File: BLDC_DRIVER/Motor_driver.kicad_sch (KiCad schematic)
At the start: 113 parts, among them IC101 DRV8323SRTAR, J104 691311400103, Q101 BSC146N10LS5ATMA1, Q102 BSC146N10LS5ATMA1, Q103 BSC146N10LS5ATMA1, Q104 BSC146N10LS5ATMA1, Q105 BSC146N10LS5ATMA1, Q106 BSC146N10LS5ATMA1

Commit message: merge fix
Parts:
- removed C102: 10n/200V, Capacitor_SMD:C_0805_2012Metric, symbol Device:C
- removed R102: 3.3R, Resistor_SMD:R_2010_5025Metric, symbol Device:R
- added C116, C117, C133: 10u, Capacitor_SMD:C_1206_3216Metric, symbol Device:C
- added C134: 10n/200V, Capacitor_SMD:C_0805_2012Metric, symbol Device:C
- added C135: 10u/100V, Capacitor_SMD:C_1210_3225Metric, symbol Device:C
- added R105: 3.3R, Resistor_SMD:R_2010_5025Metric, symbol Device:R
- C118, C119, C120, C121, C131, C132: footprint Capacitor_SMD:C_0805_2012Metric -> Capacitor_SMD:C_1206_3216Metric
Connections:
- net GND: now also C116.2, C117.2, C133.2, C135.2, R105.2
- net SLA: now also C119.2; no longer C121.2
- net SLB: now also C121.2; no longer C131.2
- net SensIA: no longer D110.2
- net SensIB: no longer D110.1
- net SensIC: no longer D111.1
- net Vdrive: now also C131.1, C116.1, C117.1, C133.1, C134.1, C135.1; no longer C119.1
- net at R107.2: now also C119.1; no longer C121.1
- net at C120.2: now also R135.2; no longer R136.1
- net at R111.2: now also C121.1; no longer C131.1
- new net: C134.2, R105.1
- new net: C131.2, R136.1
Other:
- moved on the sheet: C113, C115

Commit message: finall motor driver
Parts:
- removed L101: 1u/30A, PM4343.102NLT:INDPM140128X650N, symbol PM4343_102NLT:PM4343.102NLT
- D101, D102, D103, D104, D105, D106: footprint SBR3U60P17 -> Diode_SMD:D_PowerDI-123
- Q101, Q102, Q103, Q104, Q105, Q106: footprint BSC146N10LS5ATMA1 -> BSC146N10LS5ATMA1:BSC146N10LS5ATMA1
- TP101, TP102, TP103, TP104, TP106, TP108, TP110, TP111, TP112, TP113, TP114, TP115, TP116, TP117, TP118, TP119, TP120, TP121, TP122, TP123, TP124, TP125: footprint TestPoint:TestPoint_Pad_D2.5mm -> TestPoint:TestPoint_Pad_D1.5mm
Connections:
- net Vdrive is gone; now on net +48V: C104.1, C105.1, C106.1, C108.1, C109.1, C110.1, C113.1, C114.1, C115.1, C116.1, C117.1, C118.1, C120.1, C131.1, C133.1, C134.1, C135.1, IC101.4 (VM), IC101.5 (VDRAIN), Q101.5, Q103.5, Q105.5, R124.1, TP101.1

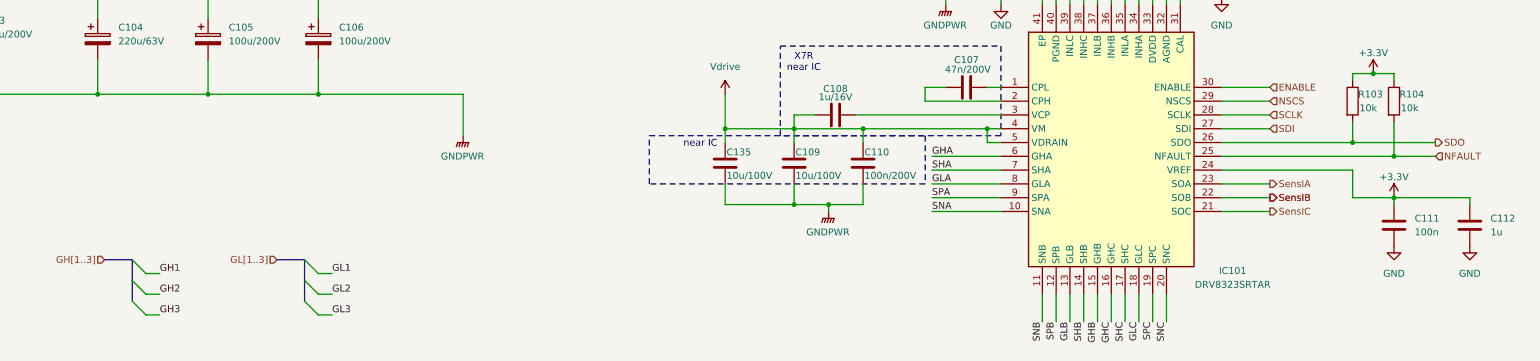
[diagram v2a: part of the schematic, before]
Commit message: board constraints added
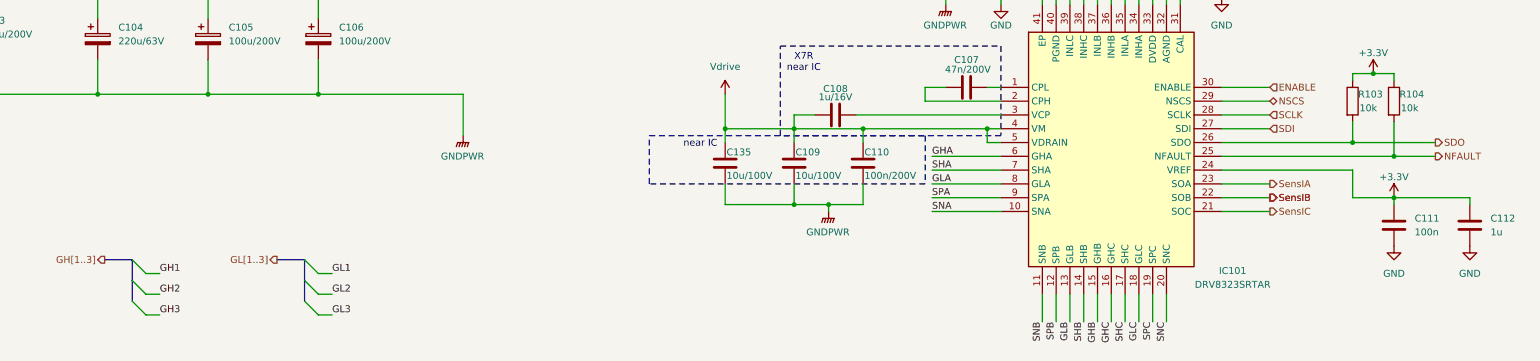
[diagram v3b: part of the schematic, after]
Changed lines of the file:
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@@
 	)
 	(hierarchical_label "NFAULT"
-		(shape input)
+		(shape output)
 		(at 302.26 73.66 0)
 		(effects
@@
 	)
 	(hierarchical_label "GH[1..3]"
-		(shape input)
+		(shape output)
 		(at 57.15 92.71 180)
 		(effects
@@
 	)
 	(hierarchical_label "GL[1..3]"
-		(shape input)
+		(shape output)
 		(at 88.9 92.71 180)
 		(effects
@@
 	)
 	(hierarchical_label "NSCS"
-		(shape input)
+		(shape bidirectional)
 		(at 271.78 63.5 0)
 		(effects

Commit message: pre layout
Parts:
- removed Q101, Q102, Q103, Q104, Q105, Q106: BSC146N10LS5ATMA1, BSC146N10LS5ATMA1:BSC146N10LS5ATMA1, symbol BSC146N10LS5ATMA1:BSC146N10LS5ATMA1
- added Q101, Q102, Q103, Q104, Q105, Q106: NTMFS4D0N08XT1G, NRVTS10100EMFST1G, symbol NTMFS4D0N08XT1G:NTMFS4D0N08XT1G
- R101: value 0R/2W -> 0R/1W; footprint Resistor_SMD:R_2010_5025Metric -> Resistor_SMD:R_0805_2012Metric
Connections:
- net +48V: now also Q101.5, Q103.5, Q105.5
- net GND: now also TP114.1, TP115.1, TP116.1
- net PVDDSENSE: now also D111.1; no longer D109.1
- net SHA: now also Q101.1, Q102.5
- net SHB: now also Q103.1, Q104.5
- net SHC: now also Q105.1, Q106.5
- net SensIA: now also D110.1
- net SensIB: now also D110.2
- net SensIC: now also D109.1
- net SensVA: now also D107.1; no longer D107.2
- net SensVB: now also D107.2; no longer D107.1
- net at D103.2, R139.2, TP102.1: now also Q103.4
- net at D104.2, R140.2, TP111.1: now also Q104.4
- net at D105.2, R141.2, TP103.1: now also Q105.4
- net at D102.2, R138.2, TP113.1: now also Q102.4
- net at D101.2, R110.2, TP104.1: now also Q101.4
- net at D106.2, R142.2, TP112.1: now also Q106.4
- net SLA renamed SPA
- net SPA: now also Q102.1; no longer TP116.1
- net SLB renamed SPB
- net SPB: now also Q104.1; no longer TP114.1
- net SLC renamed SPC
- net SPC: now also Q106.1; no longer TP115.1
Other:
- moved on the sheet: TP114, TP115, TP116

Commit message: motor driver layout v1
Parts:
- R105: footprint Resistor_SMD:R_2010_5025Metric -> Resistor_SMD:R_0805_2012Metric
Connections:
- net SensVA: now also D107.2; no longer D107.1
- net SensVB: now also D107.1; no longer D107.2
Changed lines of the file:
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@@
 	(hierarchical_label "SensVB"
 		(shape output)
-		(at 311.15 220.98 180)
+		(at 326.39 220.98 0)
 		(effects
 			(font
 				(size 1.27 1.27)
 			)
-			(justify right)
+			(justify left)
 		)
 	)
@@
 	(hierarchical_label "SensVA"
 		(shape output)
-		(at 326.39 220.98 0)
+		(at 311.15 220.98 180)
 		(effects
 			(font
 				(size 1.27 1.27)
 			)
-			(justify left)
+			(justify right)
 		)
 	)
@@
 			)
 		)
-		(property "Footprint" "Resistor_SMD:R_2010_5025Metric"
+		(property "Footprint" "Resistor_SMD:R_0805_2012Metric"
 			(at 228.092 247.65 90)
 			(effects

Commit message: mcu&power final layout
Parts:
- removed C103: 100u/200V, EMVY101ARA101MKE0S:CAPAE1300X1400N, symbol Device:C_Polarized
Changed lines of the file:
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@@
 	)
 	(junction
-		(at 30.48 41.91)
-		(diameter 0)
-		(color 0 0 0 0)
-	)
-	(junction
 		(at 45.72 167.64)
 		(diameter 0)
@@
 	)
 	(junction
-		(at 30.48 62.23)
-		(diameter 0)
-		(color 0 0 0 0)
-	)
-	(junction
 		(at 53.34 184.15)
 		(diameter 0)
@@
 	(wire
 		(pts
-			(xy 30.48 54.61) (xy 30.48 62.23)
-		)
-		(stroke
-			(width 0)
-			(type default)
-		)
-	)
-	(wire
-		(pts
 			(xy 275.59 138.43) (xy 275.59 140.97)
 		)
@@
 	(wire
 		(pts
-			(xy 30.48 46.99) (xy 30.48 41.91)
-		)
-		(stroke
-			(width 0)
-			(type default)
-		)
-	)
-	(wire
-		(pts
 			(xy 16.51 245.11) (xy 34.29 245.11)
 		)
@@
 					(unit 1)
 				)
-			)
-		)
-	)
-	(symbol
-		(lib_id "Device:C_Polarized")
-		(at 30.48 50.8 0)
-		(unit 1)
-		(exclude_from_sim no)
-		(in_bom yes)
-		(on_board yes)
-		(dnp no)
-		(fields_autoplaced yes)
-		(property "Reference" "C103"
-			(at 34.29 48.6409 0)
-			(effects
-				(font
-					(size 1.27 1.27)
-				)
-				(justify left)
-			)
-		)
-		(property "Value" "100u/200V"
-			(at 34.29 51.1809 0)
-			(effects
-				(font
-					(size 1.27 1.27)
-				)
-				(justify left)
-			)
-		)
-		(property "Footprint" "EMVY101ARA101MKE0S:CAPAE1300X1400N"
-			(at 31.4452 54.61 0)
-			(effects
-				(font
-					(size 1.27 1.27)
-				)
-				(hide yes)
-			)
-		)
-		(property "Datasheet" "~"
-			(at 30.48 50.8 0)
-			(effects
-				(font
-					(size 1.27 1.27)
-				)
-				(hide yes)
-			)
-		)
-		(property "Description" "Polarized capacitor"
-			(at 30.48 50.8 0)
-			(effects
-				(font
-					(size 1.27 1.27)
-				)
-				(hide yes)
-			)
-		)
-		(pin "2"
-		)
-		(pin "1"
-		)
-		(instances
-			(project ""
-				(path "/3fb7c58e-7fa7-4c2f-8afc-969dd7f24a74/1a6cb0fa-11a9-4eae-a722-17bc849d44a5"
-					(reference "C103")
-					(unit 1)
-				)
